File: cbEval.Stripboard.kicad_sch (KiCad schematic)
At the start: 33 parts, among them J1 Bergstik-II_3, J10 Socket.Hor.2x5.6-5535512-4, J11 Bergstik-II_3, J12 Bergstik-II_3, J13 Bergstik-II_6, J14 Bergstik-II_8, J15 Bergstik-II_6, J2 Bergstik-II_6, J3 Keystone.4918, J4 Keystone.4918, J5 Keystone.3571, J6 Keystone.3571, J7 Socket.Hor.2x5.6-5535512-4, J8 Header.Hor.2x5.9-103326-0-05, J9 Header.Hor.2x5.9-103326-0-05, U1 SN74AHC138D

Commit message: Bus-Stecker getauscht, BOM erstellt
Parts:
- removed J10, J7: Socket.Hor.2x5.6-5535512-4, BTech.Connector.AMPMODU-ModII:Socket.Hor.2x5.6-5535512-4, symbol J.AMPMODU-ModII:Socket.Hor.2x5.6-5535512-4
- removed J3, J4: Keystone.4918, BTech.Connector.QuickConnect:Keystone.4918, symbol J.QuickConnect:Keystone.4918
- removed J5, J6: Keystone.3571, BTech.Connector.QuickConnect:Keystone.3571, symbol J.QuickConnect:Keystone.3571
- removed J8, J9: Header.Hor.2x5.9-103326-0-05, Connector_PinHeader_2.54mm:PinHeader_2x05_P2.54mm_Horizontal, symbol J.AMPMODU-ModII:Header.Hor.2x5.9-103326-0-05
- added J16, J3: Header.Hor.2x8.9-103326-0-08, Connector_PinHeader_2.54mm:PinHeader_2x08_P2.54mm_Horizontal, symbol J.AMPMODU-ModII:Header.Hor.2x8.9-103326-0-08
- added J17, J4: Socket.Hor.2x8.1-5535512-8, BTech.Connector.AMPMODU-ModII:Socket.Hor.2x5.6-5535512-4, symbol J.AMPMODU-ModII:Socket.Hor.2x8.1-5535512-8
- added J5: Bergstik-II_3, Connector_PinHeader_2.54mm:PinHeader_1x03_P2.54mm_Vertical, symbol J.PinHeader:Bergstik-II_3
- MP1: footprint Symbol:KiCad-Logo2_5mm_SilkScreen -> Symbol:KiCad-Logo_5mm_SilkScreen
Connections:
- net +15V: now also J16.5, J17.5
- net +3V3: now also J16.4, J17.4
- net +5V: now also J16.3, J17.3
- net +VDC: now also J16.7, J17.7
- net -15V: now also J16.6, J17.6
- net CAN-H: now also J3.3, J4.3
- net CAN-L: now also J3.4, J4.4
- net GND: now also J16.11, J16.12, J16.13, J16.14, J16.15, J16.16, J17.11, J17.12, J17.13, J17.14, J17.15, J17.16, J3.1, J3.2, J3.5, J3.6, J4.1, J4.2, J4.5, J4.6, J5.2 (A2)
- net I2C-SCL: now also J16.10, J17.10
- net I2C-SDA: now also J16.9, J17.9
- net One-Wire: now also J3.16, J4.16
- net SPI-ADR0: now also J3.13, J4.13
- net SPI-ADR1: now also J3.14, J4.14
- net SPI-ADR2: now also J3.15, J4.15
- net SPI-CLK: now also J3.11, J4.11
- net SPI-MRST: now also J3.10, J4.10
- net SPI-MTSR: now also J3.9, J4.9
- net SPI-~CE: now also J3.12, J4.12
- net VCC: now also J16.1, J16.2, J17.1, J17.2
- net ~RESET: now also J16.8, J17.8
- new net Reserved0: J3.7, J4.7, J5.1 (A1)
- new net Reserved1: J3.8, J4.8, J5.3 (A3)
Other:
- moved on the sheet: C1, C5, H2, H3, H4, H5, H6, H7, H8, H9, J1, J11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

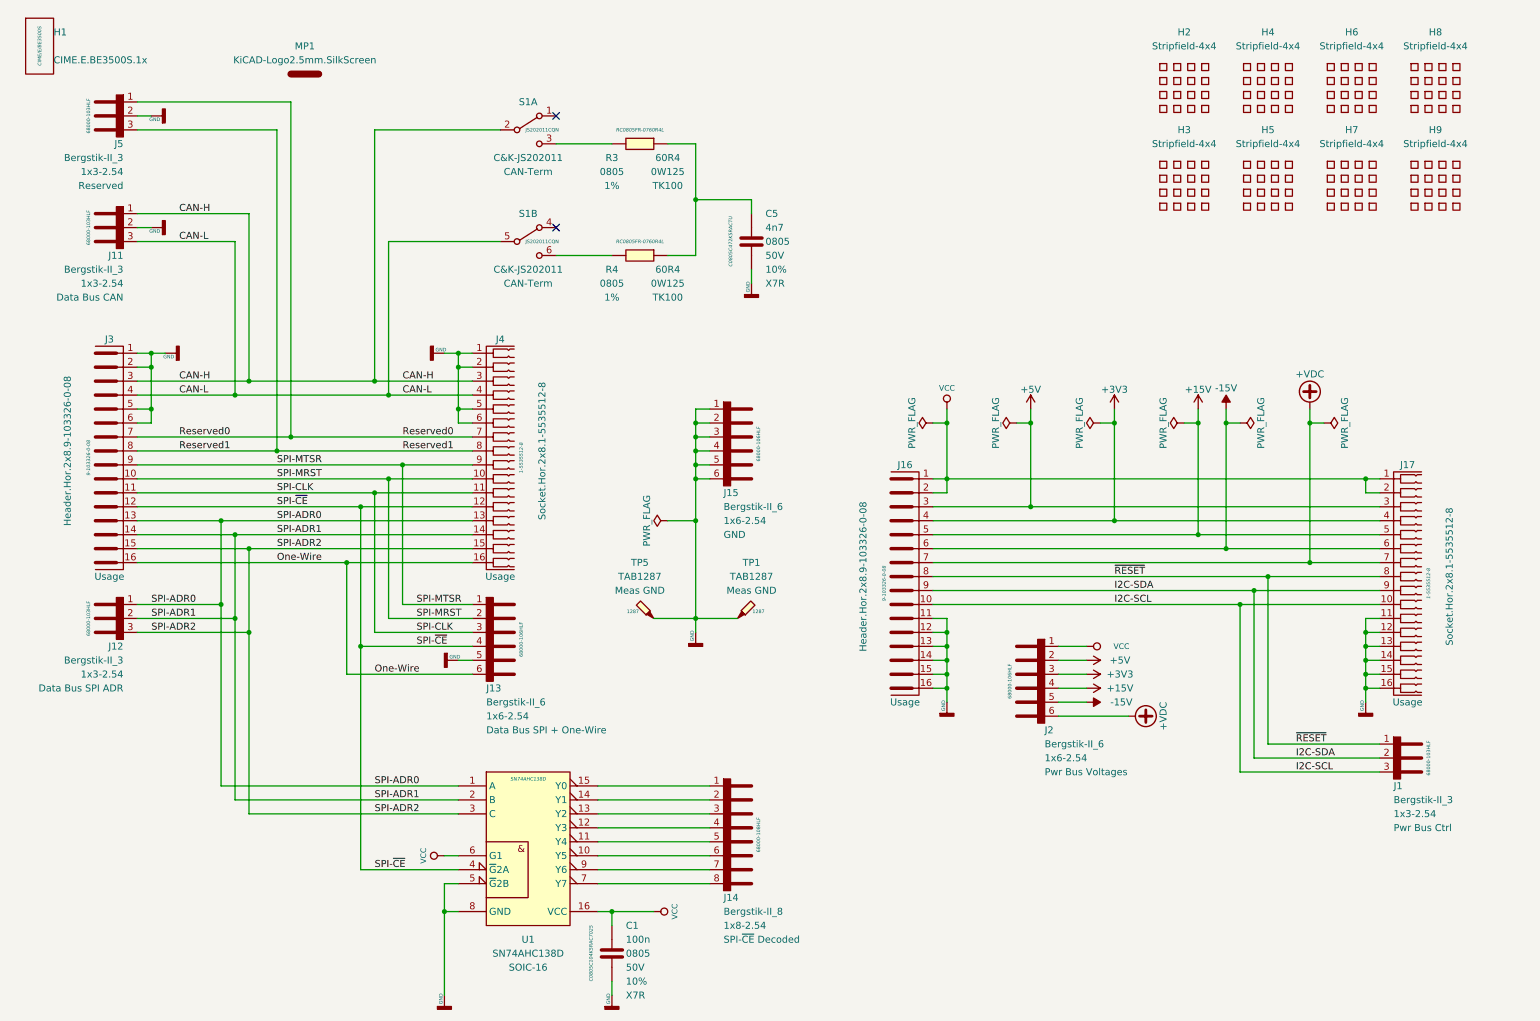
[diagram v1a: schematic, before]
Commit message: Update auf KiCAD-Version 7
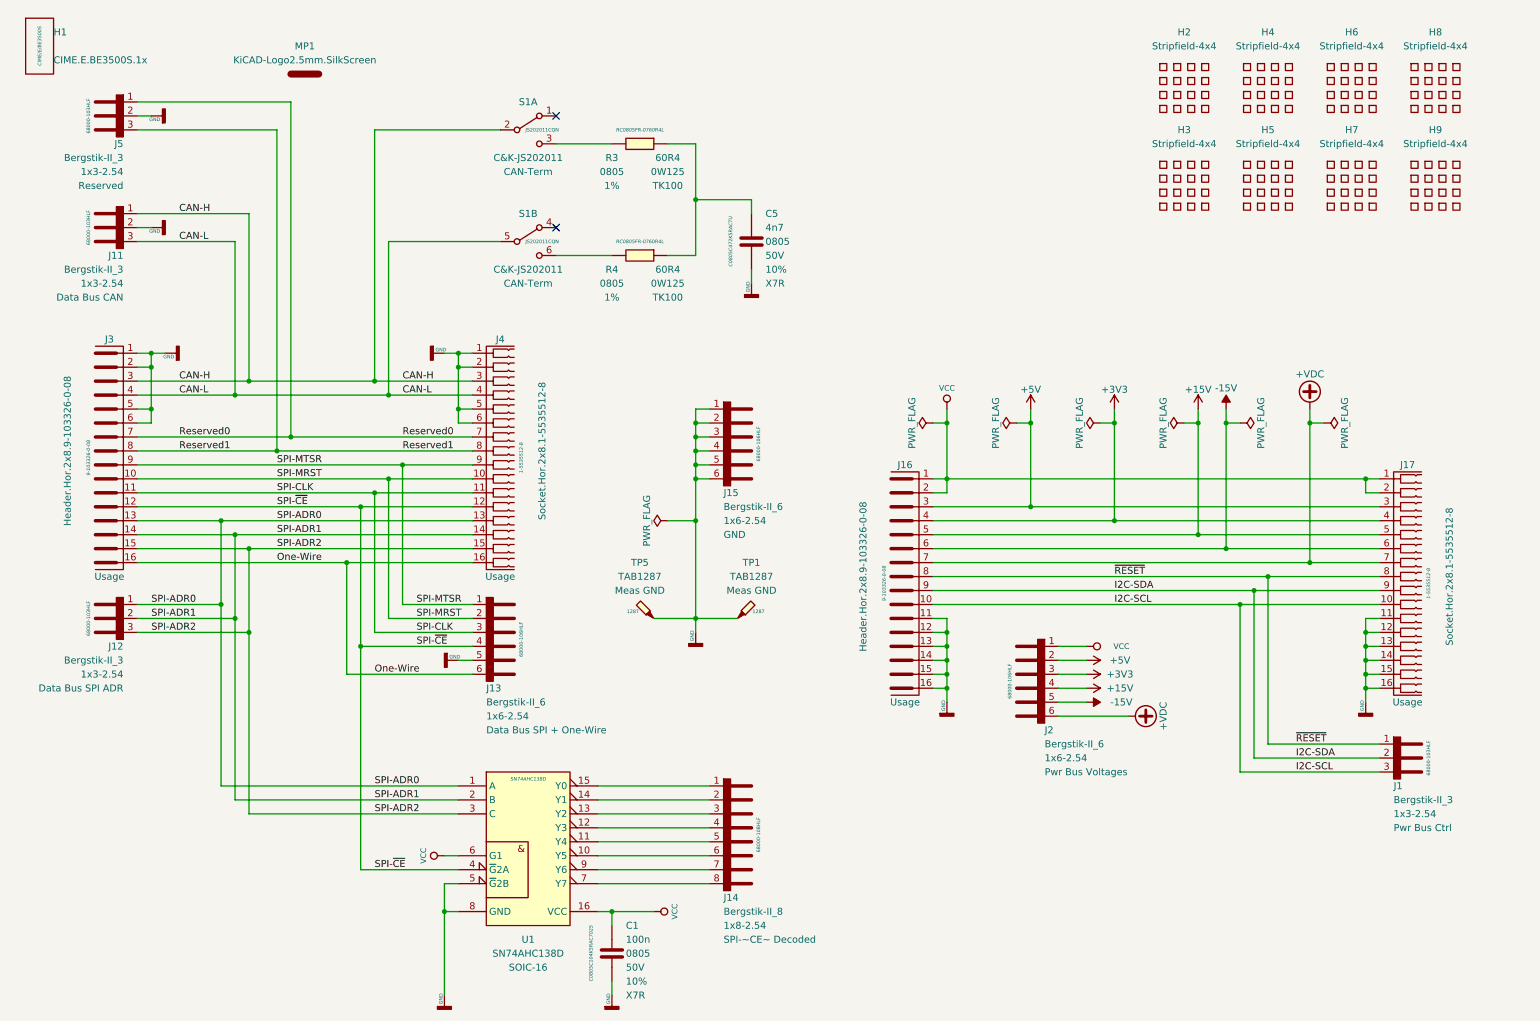
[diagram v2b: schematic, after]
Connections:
- net SPI-~CE renamed SPI-~{CE}
- net ~RESET renamed ~{RESET}
